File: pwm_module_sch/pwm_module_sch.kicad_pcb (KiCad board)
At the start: 2 copper layers, 41 parts, among them J1 SWIMM, J2 output, J3 input, Q1 AO3400, Q2 6N60, SW1 ., SW2 ., U1 TM1637, U2 STM8S003F3P, U3 LM358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

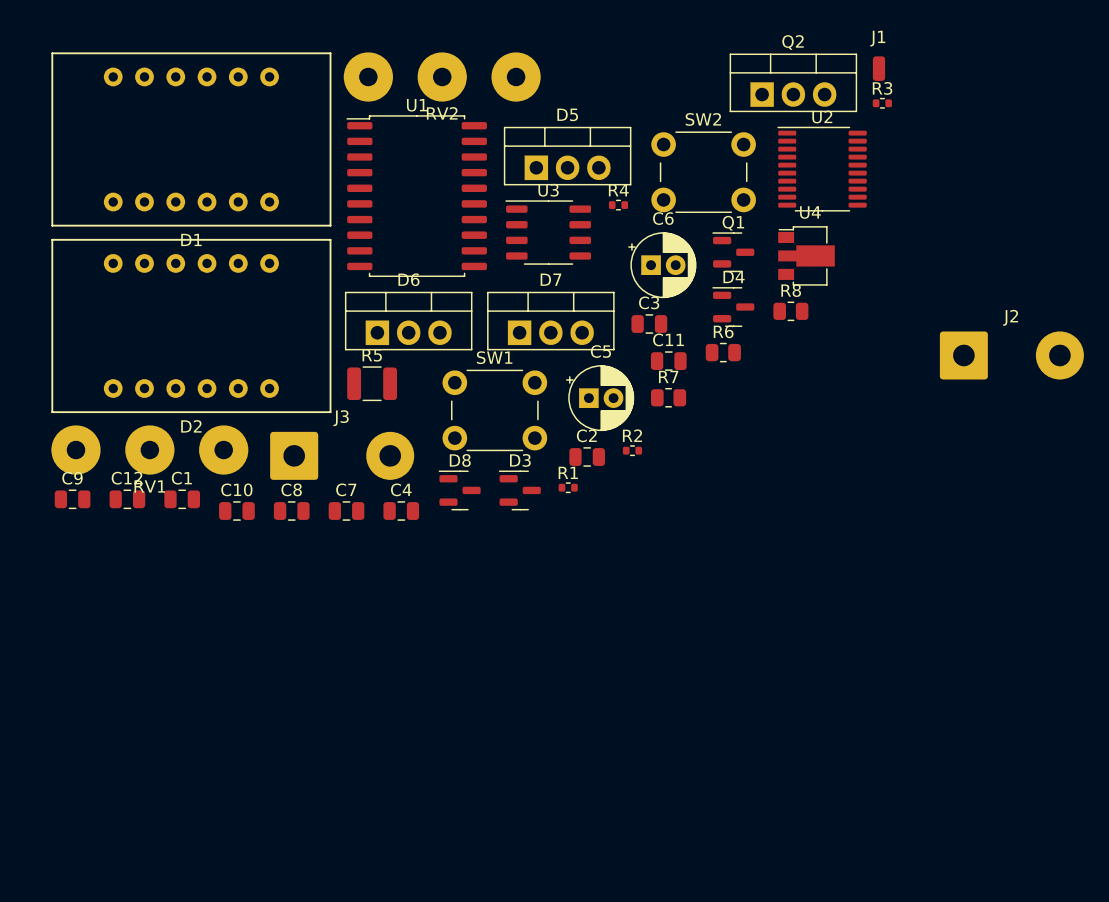
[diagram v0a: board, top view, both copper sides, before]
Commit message: one-layer PCB 6x6cm
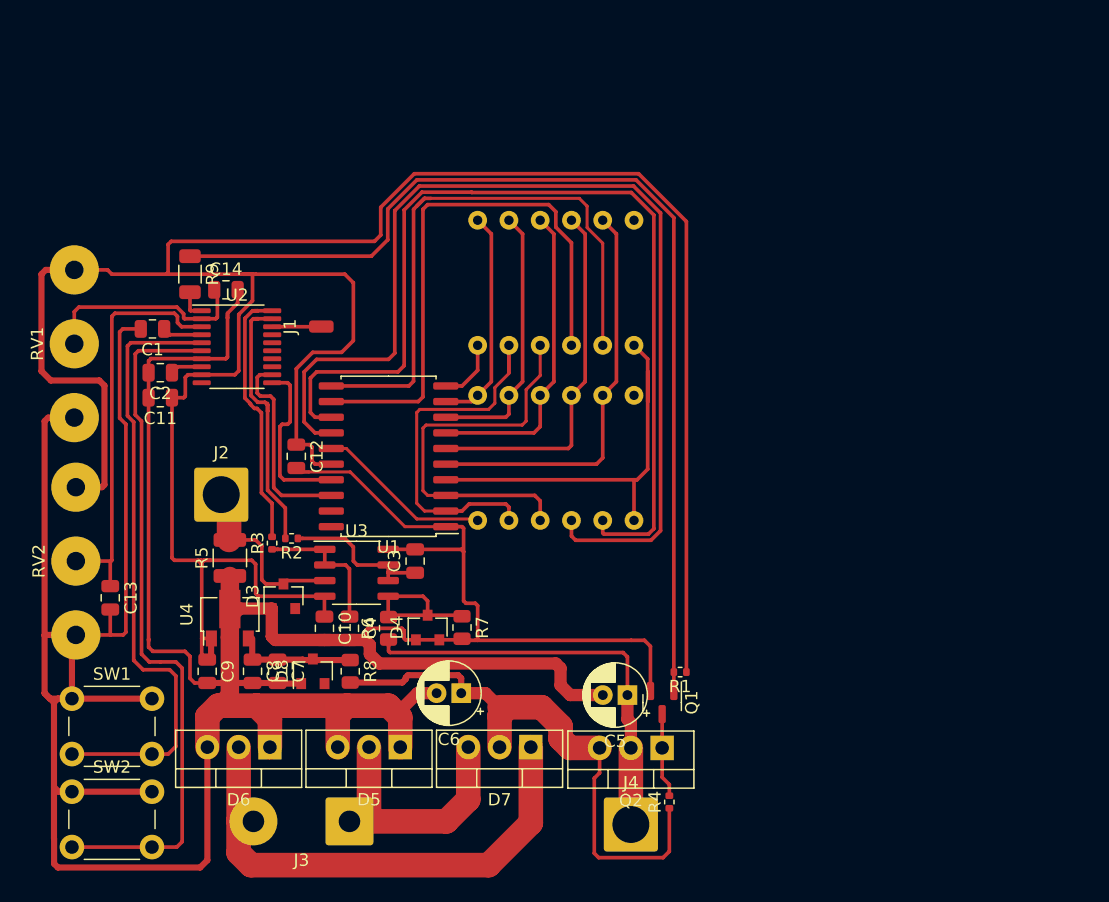
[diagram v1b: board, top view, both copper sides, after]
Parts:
- added C13: 1uF, Capacitor_SMD:C_0805_2012Metric, F.Cu at (188.7, 79.1)
- added C14: 1uF, Capacitor_SMD:C_0805_2012Metric, F.Cu at (198.1, 54.1)
- added J4: output+, Connector_Wire:SolderWire-2.5sqmm_1x01_D2.4mm_OD4.4mm, F.Cu at (231.0, 97.5)
- added R9: 75, Resistor_SMD:R_1206_3216Metric, F.Cu at (195.2, 52.8)
- D1, D2: moved to B.Cu
- D3, D4, D8: footprint Package_TO_SOT_SMD:SOT-23 -> Diode_SMD:D_SOT-23_ANK
- J2: value output -> output -; footprint Connector_Wire:SolderWire-1sqmm_1x02_P7.8mm_D1.4mm_OD3.9mm -> Connector_Wire:SolderWire-2.5sqmm_1x01_D2.4mm_OD4.4mm
- moved SW2 71.2 mm to (185.6, 94.9)
- moved J2 61.4 mm to (197.7, 70.7)
- moved R3 61.1 mm to (201.9, 74.7), turned to 90 degrees
- moved U4 55.3 mm to (198.4, 80.8), turned to 90 degrees
- moved Q2 53.7 mm to (233.6, 91.3), turned to 180 degrees
- moved J1 49.9 mm to (205.9, 57.1), turned to 90 degrees
- moved U2 49.7 mm to (199.0, 58.7)
- moved RV2 49.3 mm to (185.9, 76.1), turned to 270 degrees
- moved R4 48.7 mm to (234.1, 95.7), turned to 90 degrees
- moved D5 48.3 mm to (212.3, 91.2), turned to 180 degrees
- moved R8 46.2 mm to (208.2, 85.1), turned to 270 degrees
- moved C11 41.4 mm to (192.8, 62.9), turned to 180 degrees
- moved SW1 40.3 mm to (185.6, 87.3)
- moved C6 38.0 mm to (217.2, 86.9), turned to 180 degrees
- moved Q1 37.0 mm to (233.6, 87.6), turned to 270 degrees
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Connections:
- C5 pad 2: -VSW -> GND
- D5 pad 2: AC -> Net-(D5-Pad2)
- D6 pad 2: AC -> Net-(D6-Pad2)
- D7 pad 1: AC -> Net-(D6-Pad2)
- D7 pad 3: AC -> Net-(D5-Pad2)
- J3 pad 1: AC -> Net-(D5-Pad2)
- J3 pad 2: AC -> Net-(D6-Pad2)
- U1 pad 1: Net-(U1-Pad1) -> GND
- U1 pad 10: Net-(D1-Pad8) -> Net-(D1-Pad12)
- U1 pad 11: Net-(D1-Pad9) -> Net-(D1-Pad8)
- U1 pad 12: Net-(D1-Pad12) -> Net-(D1-Pad9)
- U2 pad 1: Net-(Q1-Pad1) -> Net-(R9-Pad2)
- U3 pad 1: Net-(C3-Pad1) -> Net-(C4-Pad1)
- U3 pad 2: Net-(C3-Pad1) -> Net-(C4-Pad1)
- U3 pad 3: Net-(D4-Pad1) -> -VSW
- U3 pad 5: -VSW -> Net-(D4-Pad1)
- U3 pad 6: Net-(C4-Pad1) -> Net-(C3-Pad1)
- U3 pad 7: Net-(C4-Pad1) -> Net-(C3-Pad1)
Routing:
- net GND: track 0.00 -> 321.1 mm
- net +3V3: track 0.00 -> 216.7 mm
- net Net-(D2-Pad9): track 0.00 -> 84.3 mm
- net Net-(Q1-Pad1): track 0.00 -> 82.8 mm
- net Net-(D2-Pad8): track 0.00 -> 77.9 mm
- net Net-(SW2-Pad2): track 0.00 -> 57.1 mm
- net Net-(SW1-Pad2): track 0.00 -> 50.3 mm
- net +24V: track 0.00 -> 49.2 mm
- net Net-(D1-Pad8): track 0.00 -> 48.3 mm
- net Net-(D6-Pad2): track 0.00 -> 47.8 mm
- net Net-(D1-Pad9): track 0.00 -> 45.4 mm
- net +VSW: track 0.00 -> 34.6 mm
- net Net-(D1-Pad5): track 0.00 -> 33.2 mm
- net Net-(D1-Pad7): track 0.00 -> 33.1 mm
- net Net-(C13-Pad1): track 0.00 -> 33.0 mm
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
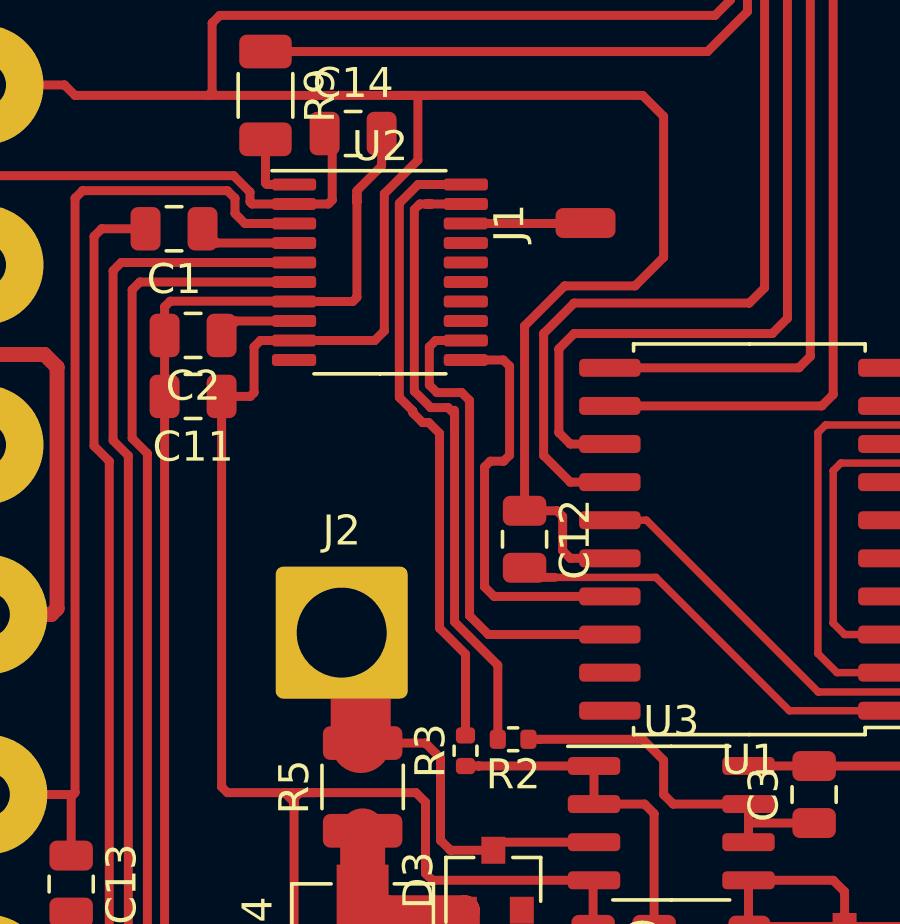
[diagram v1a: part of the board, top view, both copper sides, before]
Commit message: tm adapt, pwm add
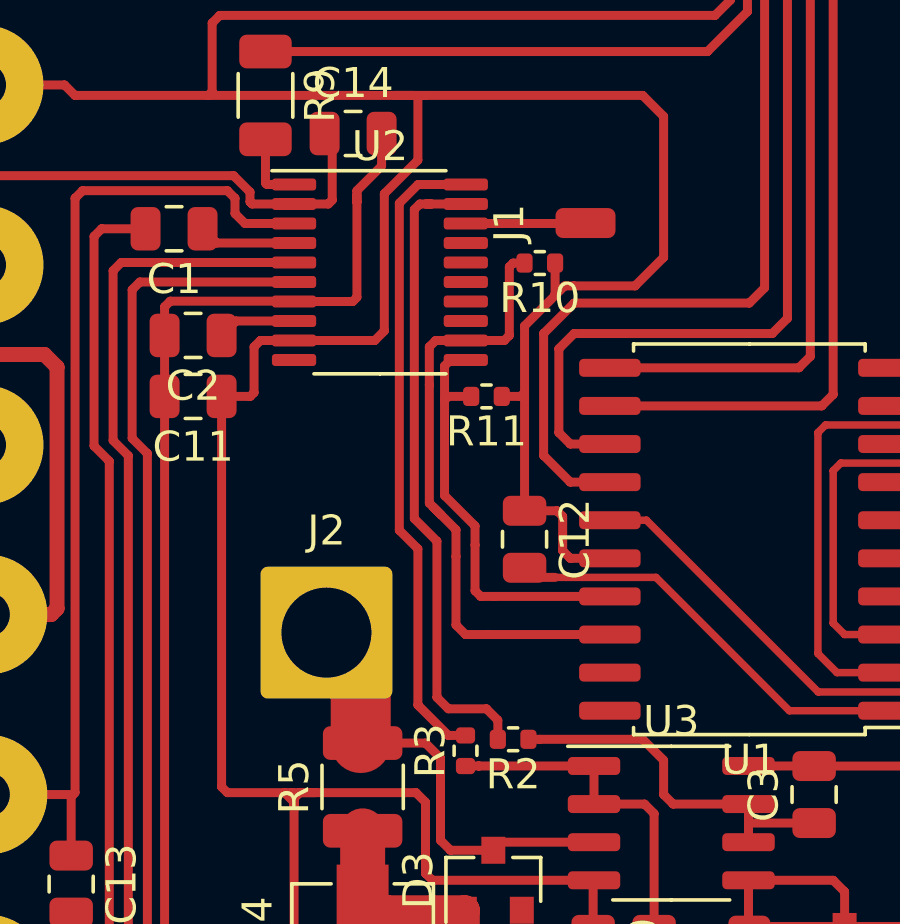
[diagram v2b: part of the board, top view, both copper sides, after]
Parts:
- added R10: 100k, Resistor_SMD:R_0402_1005Metric, F.Cu at (204.3, 58.4)
- added R11: 100k, Resistor_SMD:R_0402_1005Metric, F.Cu at (202.6, 62.9)
- moved J2 0.51 mm to (197.2, 70.7)
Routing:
- net Net-(R10-Pad2): track 16.2 -> 20.9 mm
- net +3V3: track 216.7 -> 218.5 mm
- net Net-(R11-Pad2): track 13.8 -> 14.6 mm

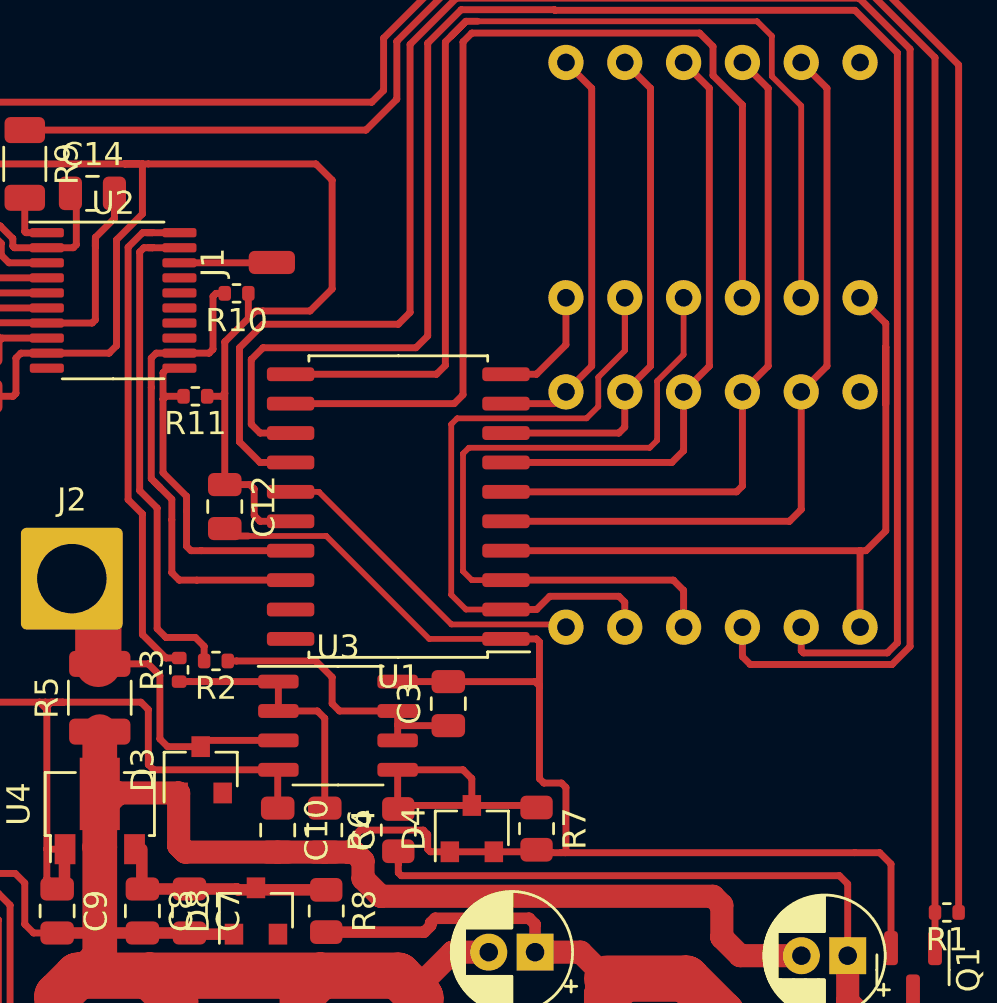
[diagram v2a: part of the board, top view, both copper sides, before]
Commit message: uart sch add
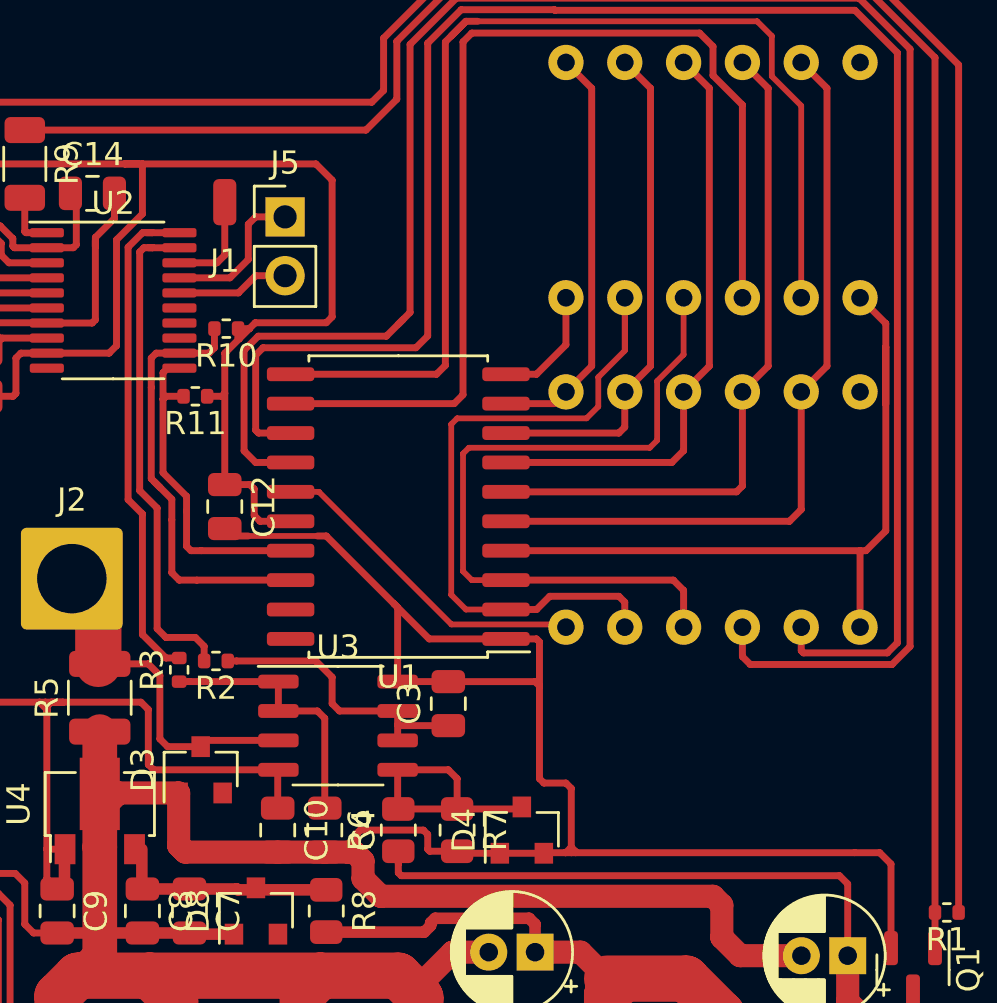
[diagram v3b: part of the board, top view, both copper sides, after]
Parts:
- added J5: uart, Connector_PinHeader_2.54mm:PinHeader_1x02_P2.54mm_Vertical, F.Cu at (206.4, 55.1)
- moved R7 3.43 mm to (213.9, 81.6)
- moved J1 3.30 mm to (203.8, 54.5), turned to 180 degrees
- moved D4 2.16 mm to (216.7, 81.6)
- moved R10 1.59 mm to (203.9, 59.9)
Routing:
- net Net-(J5-Pad1): track 0.00 -> 6.55 mm
- net Net-(J5-Pad2): track 0.00 -> 4.87 mm
- net GND: track 321.1 -> 323.8 mm
- net Net-(R10-Pad2): track 20.9 -> 19.0 mm
- net Net-(D4-Pad1): track 12.5 -> 11.5 mm

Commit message: reduced dimentions
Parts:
- added R12: 10k, Resistor_SMD:R_1210_3225Metric, F.Cu at (229.2, 84.4)
- moved R1 50.6 mm to (197.4, 51.3)
- moved R6 16.8 mm to (228.1, 81.8), turned to 180 degrees
- moved R2 11.1 mm to (198.1, 64.6), turned to 90 degrees
- moved C3 10.5 mm to (222.6, 81.2), turned to 0 degrees
- moved U3 9.34 mm to (217.1, 81.2)
- moved R3 8.52 mm to (198.9, 66.7)
- moved R7 8.31 mm to (221.8, 84.1)
- moved D4 8.30 mm to (224.6, 84.0)
- moved R11 6.66 mm to (201.3, 69.4)
- moved D2 4.69 mm to (222.7, 71.9)
- moved C12 4.69 mm to (201.6, 71.8)
- moved D1 4.69 mm to (222.7, 57.7)
- moved U1 4.69 mm to (209.1, 71.8)
- moved R5 4.63 mm to (194.2, 77.9)
- moved C4 4.06 mm to (211.6, 79.5), turned to 0 degrees
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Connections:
- U2 pad 19: Net-(R2-Pad2) -> Net-(R3-Pad2)
- U2 pad 20: Net-(R3-Pad2) -> Net-(R2-Pad2)
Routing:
- net +3V3: track 218.9 -> 156.5 mm
- net Net-(C3-Pad1): track 12.4 -> 41.9 mm
- net Net-(C4-Pad1): track 11.6 -> 29.0 mm
- net +VSW: track 34.6 -> 18.1 mm
- net -VSW: track 14.8 -> 30.0 mm
- net Net-(R2-Pad2): track 21.5 -> 11.0 mm
- net Net-(R3-Pad2): track 21.7 -> 12.0 mm
- net Net-(R11-Pad2): track 14.6 -> 19.8 mm
- net GND: track 323.8 -> 320.0 mm
- net Net-(R10-Pad2): track 19.0 -> 22.1 mm
- net Net-(D4-Pad1): track 11.5 -> 8.66 mm
- net Net-(Q1-Pad1): track 82.8 -> 80.6 mm
- net Net-(D2-Pad9): track 84.3 -> 83.6 mm

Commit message: 0402 caps
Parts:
- C1, C10, C11, C12, C3, C4: footprint Capacitor_SMD:C_0805_2012Metric -> Capacitor_SMD:C_0402_1005Metric
- moved D3 17.3 mm to (193.7, 67.9), turned to 0 degrees
- moved C10 4.68 mm to (211.6, 83.0), turned to 180 degrees
- moved R11 3.15 mm to (201.0, 72.5), turned to 270 degrees
- moved J5 1.73 mm to (206.7, 56.8)
- moved C3 1.55 mm to (221.3, 80.4), turned to 90 degrees
- moved C11 1.39 mm to (194.1, 62.4)
- moved C12 0.89 mm to (202.0, 72.5)
- moved C1 0.80 mm to (192.8, 57.7)
- moved C4 0.79 mm to (212.4, 79.3), turned to 180 degrees
- moved R2 0.32 mm to (198.4, 64.6)
- moved R1 0.30 mm to (197.4, 51.0)
- moved R9 0.29 mm to (195.2, 52.5)
- moved J1 0.25 mm to (203.9, 54.7)
- moved J2 0.06 mm to (195.5, 72.8)
- moved R5 0.06 mm to (194.2, 77.8)
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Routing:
- net GND: track 320.0 -> 328.7 mm
- net Net-(C3-Pad1): track 41.9 -> 39.0 mm
- net -VSW: track 30.0 -> 33.0 mm
- net Net-(D2-Pad8): track 77.7 -> 79.7 mm
- net Net-(C4-Pad1): track 29.0 -> 30.6 mm
- net +3V3: track 156.5 -> 158.1 mm
- net Net-(C14-Pad1): track 18.7 -> 17.3 mm
- net Net-(C13-Pad1): track 33.0 -> 31.6 mm
- net Net-(J5-Pad1): track 6.55 -> 5.20 mm
- net Net-(D2-Pad9): track 83.6 -> 84.4 mm
